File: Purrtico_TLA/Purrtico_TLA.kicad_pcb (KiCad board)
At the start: 2 copper layers, 100 x 50 mm, 65 parts, among them J1 XLR3, J2 Conn_01x03, J3 Conn_01x02, J4 XLR3, J5 Conn_01x02, U1 OPA1679, U2 OPA1679

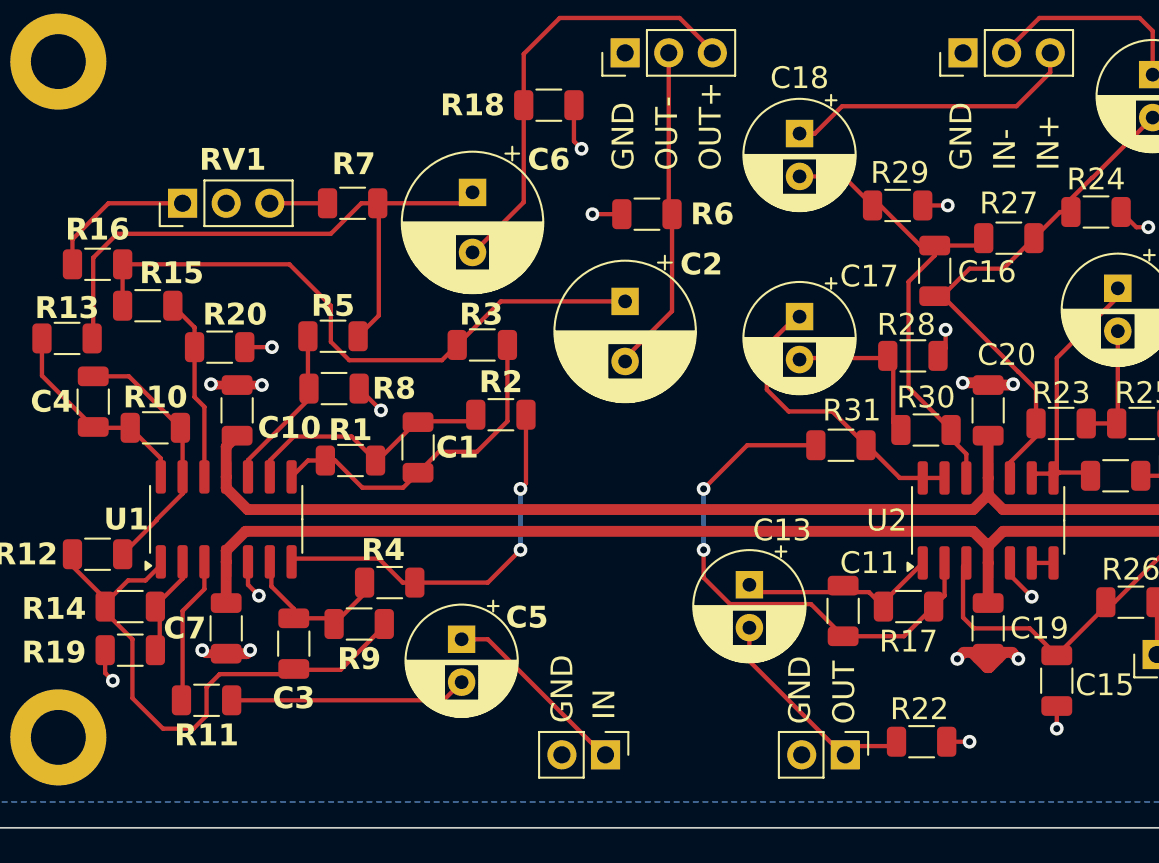
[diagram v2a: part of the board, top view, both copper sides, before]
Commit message: input trim & teardrops
replaced 560R resistor with a 10k trim pot, added teardrops to THT- & IC-Pads
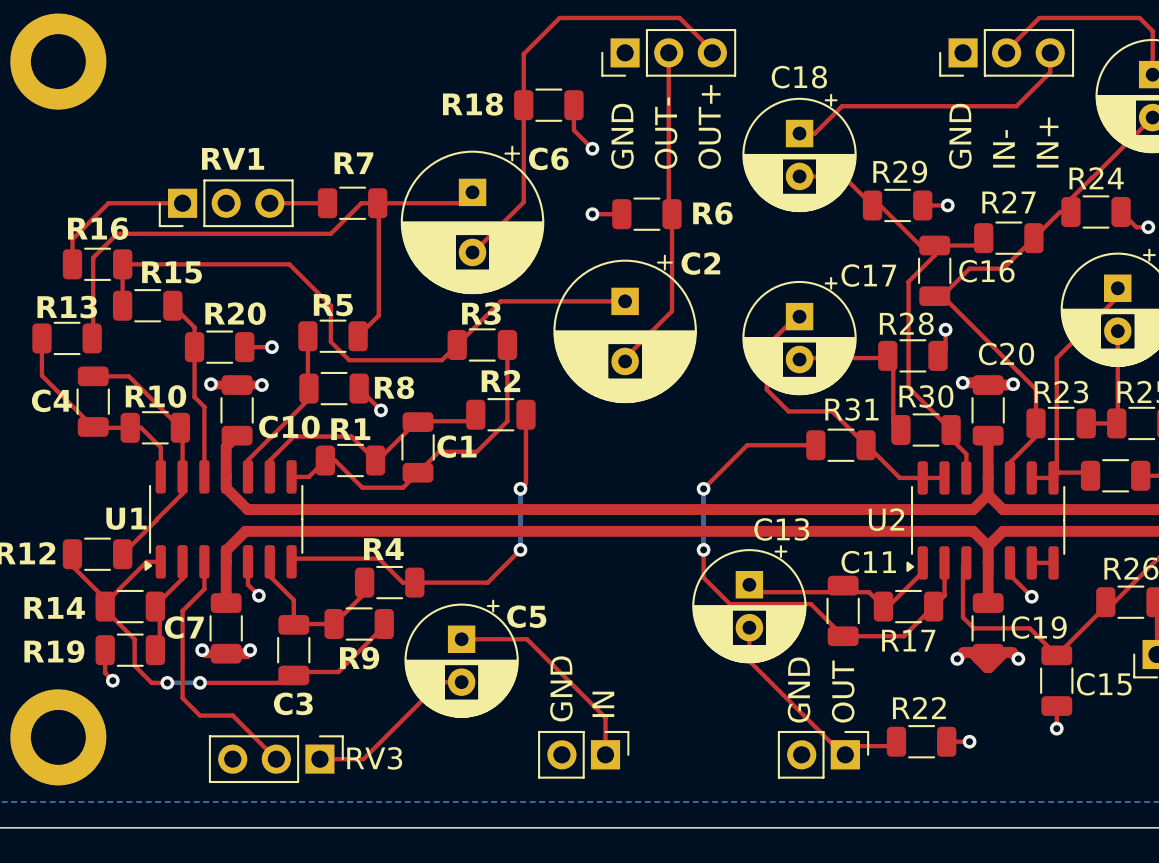
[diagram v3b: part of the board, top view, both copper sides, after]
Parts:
- removed R11: 560R, Resistor_SMD:R_1206_3216Metric
- added RV3: 10k, Connector_PinHeader_2.54mm:PinHeader_1x03_P2.54mm_Vertical, F.Cu at (63.5, 127.0)
- moved C3 0.38 mm to (62.0, 120.7)
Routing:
- net Net-(U1A-+): track 8.62 -> 15.4 mm
- net Net-(C3-Pad1): track 34.5 -> 30.5 mm, vias 0 -> 2
- net Net-(C5-Pad2): track 13.8 -> 10.1 mm
- net Net-(J3-Pin_1): track 11.2 -> 12.4 mm

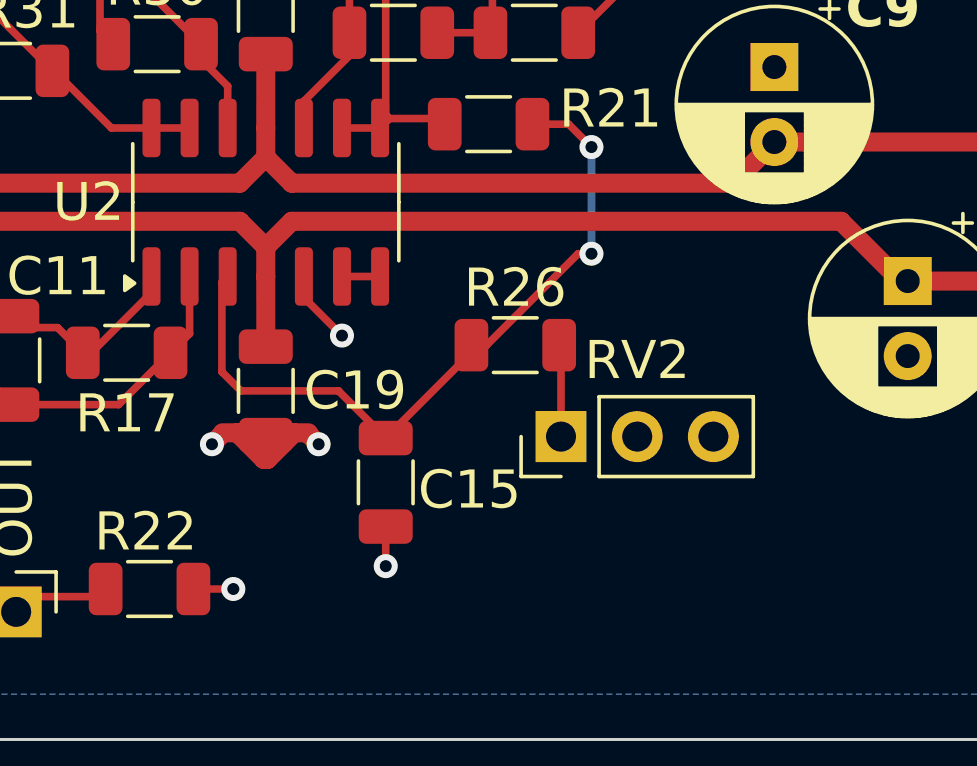
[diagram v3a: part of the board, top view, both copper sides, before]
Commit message: added 0R resistors
added 0R resistors to make the unused opamp potentially usable
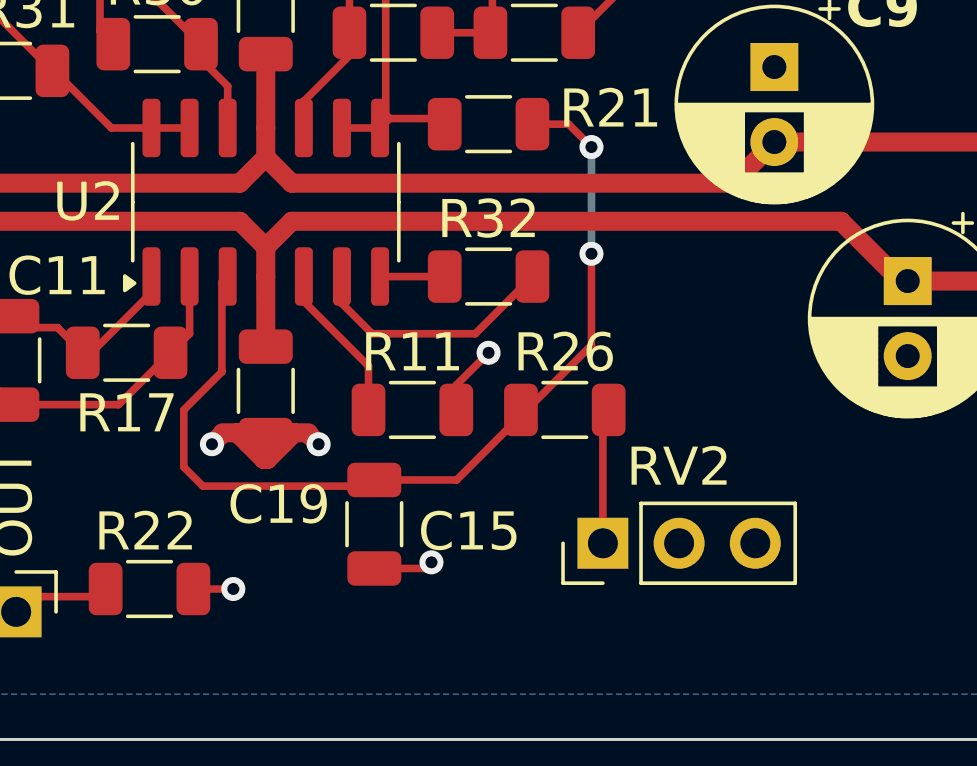
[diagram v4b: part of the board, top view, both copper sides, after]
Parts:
- added R11: 0R, Resistor_SMD:R_1206_3216Metric, F.Cu at (107.3, 120.0)
- added R32: 1k, Resistor_SMD:R_1206_3216Metric, F.Cu at (109.9, 115.6)
- moved RV2 3.82 mm to (113.7, 124.5)
- moved R26 2.72 mm to (112.4, 120.0)
- moved C15 1.45 mm to (106.0, 123.8)
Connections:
- U2 pad 5: GND -> Net-(U2B-+)
- U2 pad 7: Net-(U2B--) -> Net-(R32-Pad1)
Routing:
- net Net-(U2B--): track 1.27 -> 8.46 mm
- net Net-(U2A-+): track 25.0 -> 31.8 mm
- net Net-(U2B-+): track 0.00 -> 5.34 mm
- net Net-(R32-Pad1): track 0.00 -> 2.16 mm
- net Net-(R26-Pad1): track 3.07 -> 4.52 mm
- net GND: track 39.6 -> 40.1 mm

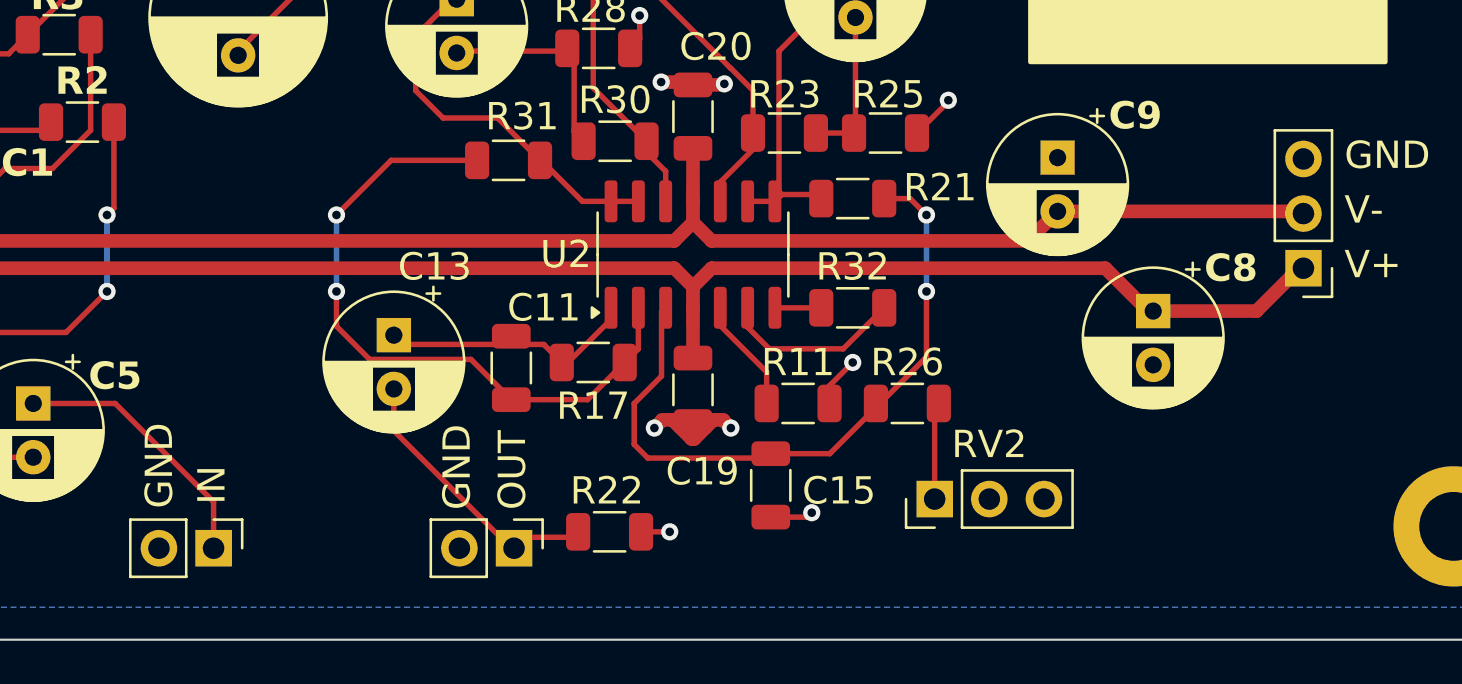
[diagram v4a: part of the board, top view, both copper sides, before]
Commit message: started purrtico m eq
singla band only, for testing
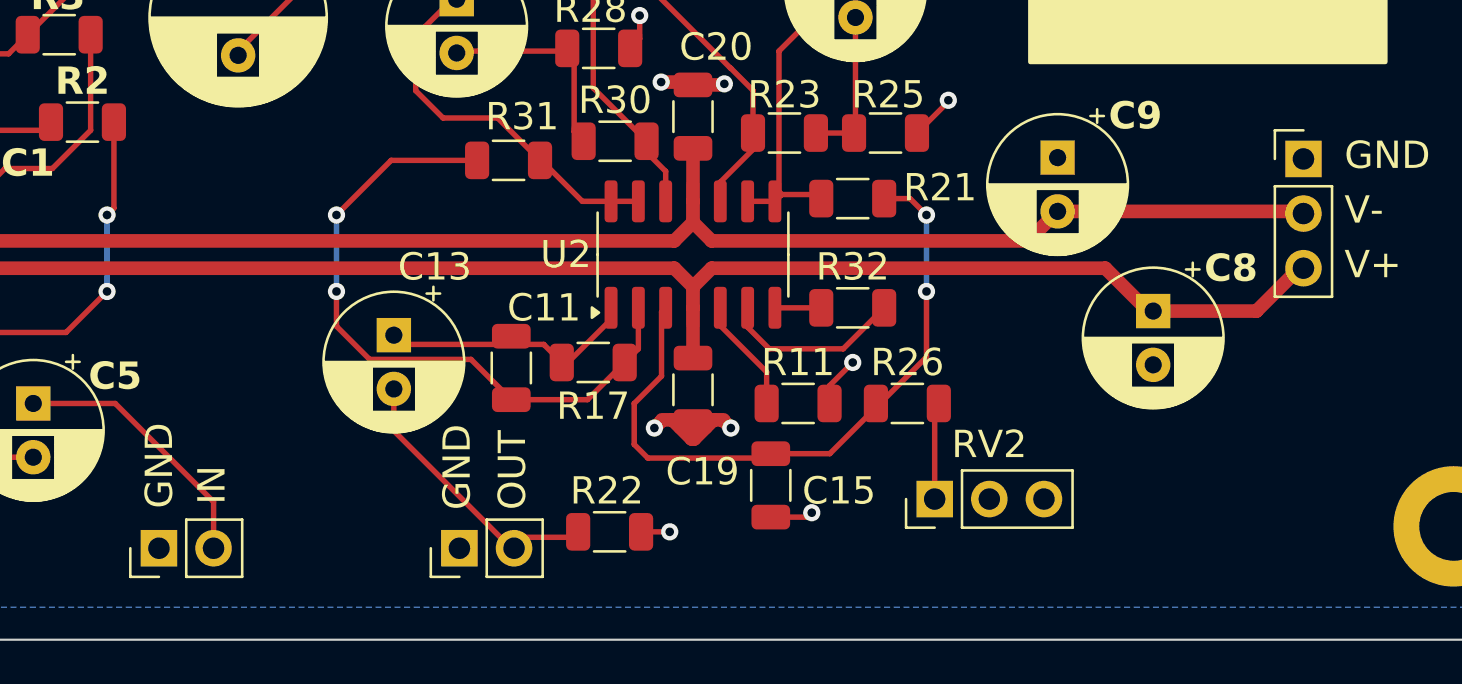
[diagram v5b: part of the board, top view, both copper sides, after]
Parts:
- moved J2 5.08 mm to (130.8, 108.6), turned to 0 degrees
- moved J3 2.54 mm to (77.6, 126.7), turned to 90 degrees
- moved J5 2.54 mm to (91.6, 126.7), turned to 90 degrees
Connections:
- C13 pad 2: Net-(J5-Pin_1) -> Net-(J5-Pin_2)
- C5 pad 1: Net-(J3-Pin_1) -> Net-(J3-Pin_2)
- J2 pad 1: +15V -> GND
- J2 pad 3: GND -> +15V
- J3 pad 1: Net-(J3-Pin_1) -> GND
- J3 pad 2: GND -> Net-(J3-Pin_2)
- J5 pad 1: Net-(J5-Pin_1) -> GND
- J5 pad 2: GND -> Net-(J5-Pin_2)
- R22 pad 2: Net-(J5-Pin_1) -> Net-(J5-Pin_2)
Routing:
- net Net-(J5-Pin_2): track 0.00 -> 13.1 mm
- net Net-(J5-Pin_1): track 13.1 -> 0.00 mm
- net Net-(J3-Pin_2): track 0.00 -> 12.4 mm
- net Net-(J3-Pin_1): track 12.4 -> 0.00 mm

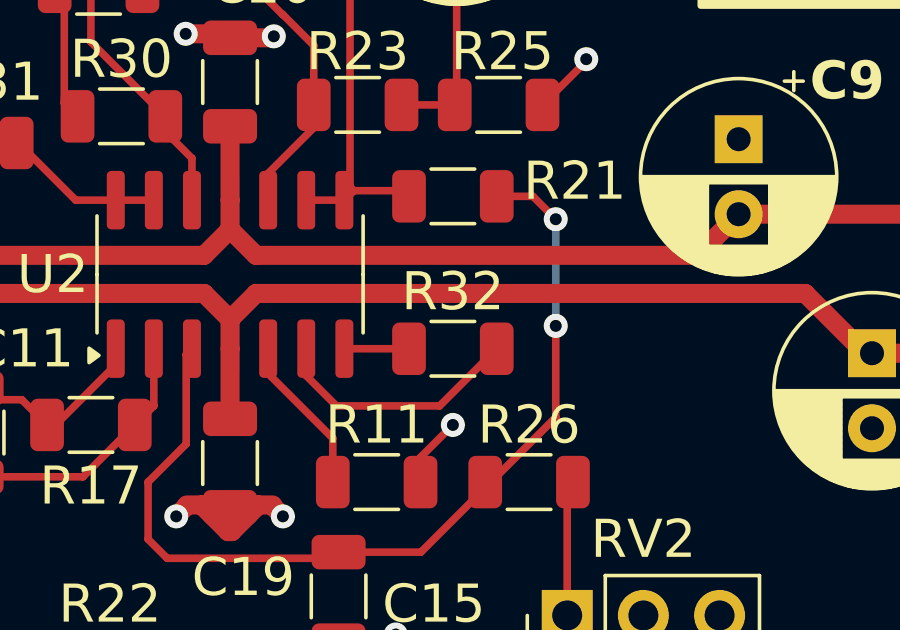
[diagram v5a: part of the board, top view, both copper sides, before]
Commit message: update 0R resistors
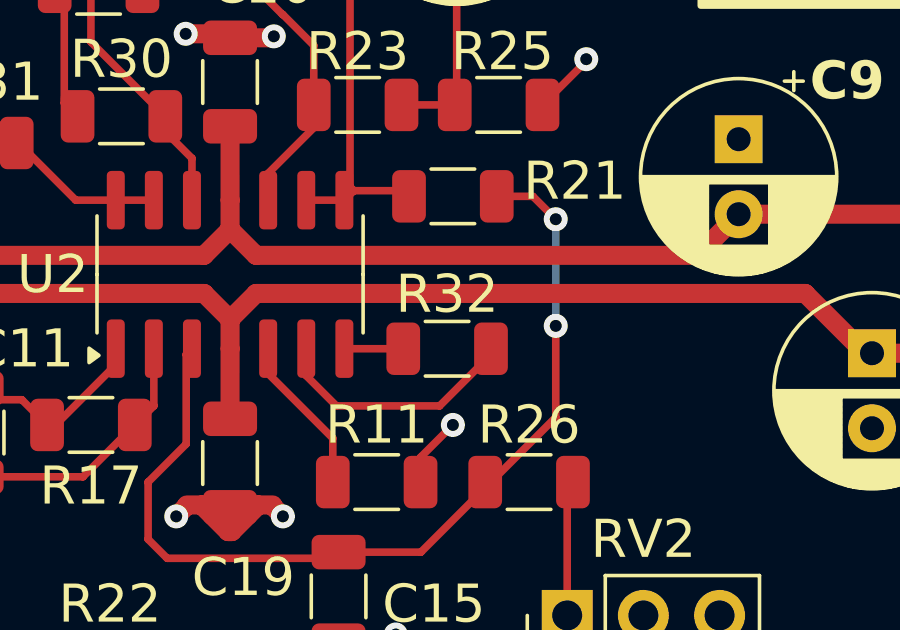
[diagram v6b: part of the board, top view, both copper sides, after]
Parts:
- R32: value 1k -> 0R
- moved R32 0.19 mm to (109.7, 115.6)
